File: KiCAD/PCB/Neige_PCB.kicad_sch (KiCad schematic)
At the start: 89 parts, among them J1 TYPE-C 16PIN 2MD(073), SW1 SW_Push, SW10 SW_Push, SW11 SW_Push, SW12 SW_Push, SW13 SW_Push, SW14 SW_Push, SW15 SW_Push, SW16 SW_Push, SW17 SW_Push, SW18 SW_Push, SW19 SW_Push, SW2 SW_Push, SW20 SW_Push, SW21 SW_Push, SW22 SW_Push, SW23 SW_Push, SW24 SW_Push, SW25 SW_Push, SW26 SW_Push, SW27 SW_Push, SW28 SW_Push, SW29 SW_Push, SW3 SW_Push, SW30 SW_Push, SW31 SW_Push, SW32 SW_Push, SW33 SW_Push, SW34 SW_Push, SW35 SW_Push, SW36 SW_Push, SW4 SW_Push, SW5 SW_Push, SW6 SW_Push, SW7 SW_Push, SW8 SW_Push, SW9 SW_Push, U1 USBLC6-2SC6, U2 XC6206P332MR, U3 STM32F072CBU6

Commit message: v1.0
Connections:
- net XIN: no longer names the net of U3.5 (PF0)
- net XOUT: no longer names the net of U3.6 (PF1)
- no-connect marks 20 -> 22
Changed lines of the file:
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@@
+	)
+	(no_connect
+		(at 203.2 161.29)
 	)
 	(no_connect
@@
 	(no_connect
 		(at 203.2 184.15)
+	)
+	(no_connect
+		(at 203.2 158.75)
 	)
 	(no_connect
@@
 		)
 	)
-	(global_label "XOUT"
-		(shape input)
-		(at 203.2 161.29 180)
+	(global_label "COL8"
+		(shape input)
+		(at 203.2 176.53 180)
 		(fields_autoplaced yes)
 		(effects
@@
 		)
 		(property "Intersheetrefs" "${INTERSHEET_REFS}"
-			(at 195.4561 161.29 0)
+			(at 195.3767 176.53 0)
 			(effects
 				(font
@@
 		)
 	)
+	(global_label "COL7"
+		(shape input)
+		(at 191.77 33.02 90)
+		(fields_autoplaced yes)
+		(effects
+			(font
+				(size 1.27 1.27)
+			)
+			(justify left)
+		)
+		(property "Intersheetrefs" "${INTERSHEET_REFS}"
+			(at 191.77 25.1967 90)
+			(effects
+				(font
+					(size 1.27 1.27)
+				)
+				(justify left)
+				(hide yes)
+			)
+		)
+	)
+	(global_label "COL11"
+		(shape input)
+		(at 283.21 33.02 90)
+		(fields_autoplaced yes)
+		(effects
+			(font
+				(size 1.27 1.27)
+			)
+			(justify left)
+		)
+		(property "Intersheetrefs" "${INTERSHEET_REFS}"
+			(at 283.21 23.9872 90)
+			(effects
+				(font
+					(size 1.27 1.27)
+				)
+				(justify left)
+				(hide yes)
+			)
+		)
+	)
 	(global_label "COL8"
 		(shape input)
-		(at 203.2 176.53 180)
+		(at 214.63 33.02 90)
+		(fields_autoplaced yes)
+		(effects
+			(font
+				(size 1.27 1.27)
+			)
+			(justify left)
+		)
+		(property "Intersheetrefs" "${INTERSHEET_REFS}"
+			(at 214.63 25.1967 90)
+			(effects
+				(font
+					(size 1.27 1.27)
+				)
+				(justify left)
+				(hide yes)
+			)
+		)
+	)
+	(global_label "COL2"
+		(shape input)
+		(at 77.47 33.02 90)
+		(fields_autoplaced yes)
+		(effects
+			(font
+				(size 1.27 1.27)
+			)
+			(justify left)
+		)
+		(property "Intersheetrefs" "${INTERSHEET_REFS}"
+			(at 77.3906 25.7688 90)
+			(effects
+				(font
+					(size 1.27 1.27)
+				)
+				(justify left)
+				(hide yes)
+			)
+		)
+	)
+	(global_label "COL5"
+		(shape input)
+		(at 146.05 33.02 90)
+		(fields_autoplaced yes)
+		(effects
+			(font
+				(size 1.27 1.27)
+			)
+			(justify left)
+		)
+		(property "Intersheetrefs" "${INTERSHEET_REFS}"
+			(at 146.05 25.1967 90)
+			(effects
+				(font
+					(size 1.27 1.27)
+				)
+				(justify left)
+				(hide yes)
+			)
+		)
+	)
+	(global_label "ROW0"
+		(shape input)
+		(at 27.94 49.53 180)
 		(fields_autoplaced yes)
 		(effects
@@
 		)
 		(property "Intersheetrefs" "${INTERSHEET_REFS}"
-			(at 195.3767 176.53 0)
+			(at 19.6934 49.53 0)
 			(effects
 				(font
@@
 		)
 	)
-	(global_label "COL7"
-		(shape input)
-		(at 191.77 33.02 90)
+	(global_label "COL1"
+		(shape input)
+		(at 54.61 33.02 90)
 		(fields_autoplaced yes)
 		(effects
@@
 		)
 		(property "Intersheetrefs" "${INTERSHEET_REFS}"
-			(at 191.77 25.1967 90)
+			(at 54.5306 25.7688 90)
 			(effects
 				(font
@@
 		)
 	)
-	(global_label "COL11"
-		(shape input)
-		(at 283.21 33.02 90)
+	(global_label "ROW2"
+		(shape input)
+		(at 27.94 82.55 180)
+		(fields_autoplaced yes)
+		(effects
+			(font
+				(size 1.27 1.27)
+			)
+			(justify right)
+		)
+		(property "Intersheetrefs" "${INTERSHEET_REFS}"
+			(at 19.6934 82.55 0)
+			(effects
+				(font
+					(size 1.27 1.27)
+				)
+				(justify right)
+				(hide yes)
+			)
+		)
+	)
+	(global_label "ROW1"
+		(shape input)
+		(at 203.2 181.61 180)
+		(fields_autoplaced yes)
+		(effects
+			(font
+				(size 1.27 1.27)
+			)
+			(justify right)
+		)
+		(property "Intersheetrefs" "${INTERSHEET_REFS}"
+			(at 194.9534 181.61 0)
+			(effects
+				(font
+					(size 1.27 1.27)
+				)
+				(justify right)
+				(hide yes)
+			)
+		)
+	)
+	(global_label "BOOT"
+		(shape input)
+		(at 127 212.09 0)
 		(fields_autoplaced yes)
 		(effects
@@
 		)
 		(property "Intersheetrefs" "${INTERSHEET_REFS}"
-			(at 283.21 23.9872 90)
+			(at 134.8838 212.09 0)
 			(effects
 				(font
@@
 		)
 	)
-	(global_label "COL8"
-		(shape input)
-		(at 214.63 33.02 90)
+	(global_label "COL0"
+		(shape input)
+		(at 31.75 33.02 90)
 		(fields_autoplaced yes)
 		(effects
@@
 		)
 		(property "Intersheetrefs" "${INTERSHEET_REFS}"
-			(at 214.63 25.1967 90)
+			(at 31.6706 25.7688 90)
 			(effects
 				(font
@@
 		)
 	)
-	(global_label "COL2"
-		(shape input)
-		(at 77.47 33.02 90)
+	(global_label "COL10"
+		(shape input)
+		(at 260.35 33.02 90)
 		(fields_autoplaced yes)
 		(effects
@@
 		)
 		(property "Intersheetrefs" "${INTERSHEET_REFS}"
-			(at 77.3906 25.7688 90)
+			(at 260.35 23.9872 90)
 			(effects
 				(font
@@
 				(hide yes)
 			)
-		)
-	)
-	(global_label "COL5"
-		(shape input)
-		(at 146.05 33.02 90)
-		(fields_autoplaced yes)
-		(effects
-			(font
-				(size 1.27 1.27)
-			)
-			(justify left)
-		)
-		(property "Intersheetrefs" "${INTERSHEET_REFS}"
-			(at 146.05 25.1967 90)
-			(effects
-				(font
-					(size 1.27 1.27)
-				)
-				(justify left)
-				(hide yes)
-			)
-		)
-	)
-	(global_label "ROW0"
-		(shape input)
-		(at 27.94 49.53 180)
-		(fields_autoplaced yes)
-		(effects
-			(font
-				(size 1.27 1.27)
-			)
-			(justify right)
-		)
-		(property "Intersheetrefs" "${INTERSHEET_REFS}"
-			(at 19.6934 49.53 0)
-			(effects
-				(font
-					(size 1.27 1.27)
-				)
-				(justify right)
-				(hide yes)
-			)
-		)
-	)
-	(global_label "COL1"
-		(shape input)
-		(at 54.61 33.02 90)
-		(fields_autoplaced yes)
-		(effects
-			(font
-				(size 1.27 1.27)
-			)
-			(justify left)
-		)
-		(property "Intersheetrefs" "${INTERSHEET_REFS}"
-			(at 54.5306 25.7688 90)
-			(effects
-				(font
-					(size 1.27 1.27)
-				)
-				(justify left)
-				(hide yes)
-			)
-		)
-	)
-	(global_label "ROW2"
-		(shape input)
-		(at 27.94 82.55 180)
-		(fields_autoplaced yes)
-		(effects
-			(font
-				(size 1.27 1.27)
-			)
-			(justify right)
-		)
-		(property "Intersheetrefs" "${INTERSHEET_REFS}"
-			(at 19.6934 82.55 0)
-			(effects
-				(font
-					(size 1.27 1.27)
-				)
-				(justify right)
-				(hide yes)
-			)
-		)
-	)
-	(global_label "ROW1"
-		(shape input)
-		(at 203.2 181.61 180)
-		(fields_autoplaced yes)
-		(effects
-			(font
-				(size 1.27 1.27)
-			)
-			(justify right)
-		)
-		(property "Intersheetrefs" "${INTERSHEET_REFS}"
-			(at 194.9534 181.61 0)
-			(effects
-				(font
-					(size 1.27 1.27)
-				)
-				(justify right)
-				(hide yes)
-			)
-		)
-	)
-	(global_label "BOOT"
-		(shape input)
-		(at 127 212.09 0)
-		(fields_autoplaced yes)
-		(effects
-			(font
-				(size 1.27 1.27)
-			)
-			(justify left)
-		)
-		(property "Intersheetrefs" "${INTERSHEET_REFS}"
-			(at 134.8838 212.09 0)
-			(effects
-				(font
-					(size 1.27 1.27)
-				)
-				(justify left)
-				(hide yes)
-			)
-		)
-	)
-	(global_label "COL0"
-		(shape input)
-		(at 31.75 33.02 90)
-		(fields_autoplaced yes)
-		(effects
-			(font
-				(size 1.27 1.27)
-			)
-			(justify left)
-		)
-		(property "Intersheetrefs" "${INTERSHEET_REFS}"
-			(at 31.6706 25.7688 90)
-			(effects
-				(font
-					(size 1.27 1.27)
-				)
-				(justify left)
-				(hide yes)
-			)
-		)
-	)
-	(global_label "COL10"
-		(shape input)
-		(at 260.35 33.02 90)
-		(fields_autoplaced yes)
-		(effects
-			(font
-				(size 1.27 1.27)
-			)
-			(justify left)
-		)
-		(property "Intersheetrefs" "${INTERSHEET_REFS}"
-			(at 260.35 23.9872 90)
-			(effects
-				(font
-					(size 1.27 1.27)
-				)
-				(justify left)
-				(hide yes)
-			)
-		)
-	)
-	(global_label "XIN"
-		(shape input)
-		(at 203.2 158.75 180)
-		(fields_autoplaced yes)
-		(effects
-			(font
-				(size 1.27 1.27)
-			)
-			(justify right)
-		)
-		(property "Intersheetrefs" "${INTERSHEET_REFS}"
-			(at 197.1494 158.75 0)
-			(effects
-				(font
-					(size 1.27 1.27)
-				)
-				(justify right)
-				(hide yes)
-			)

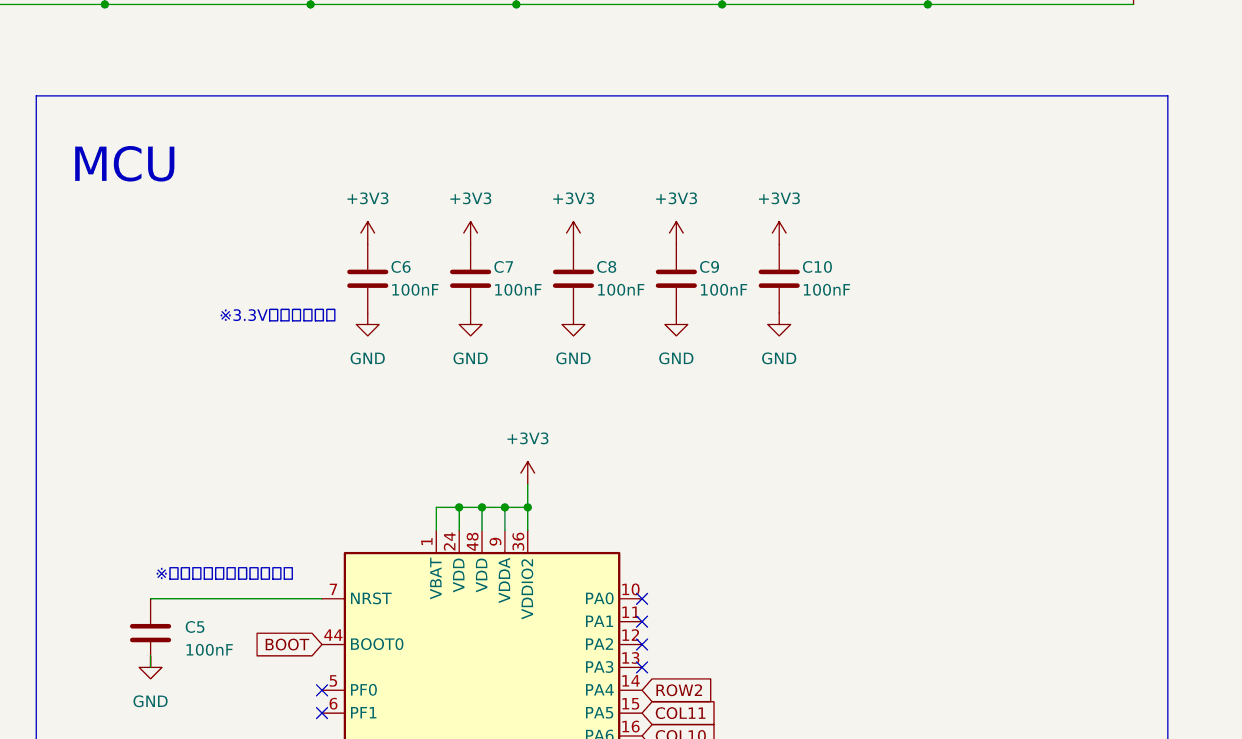
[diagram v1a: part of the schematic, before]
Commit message: パスコン見直し版
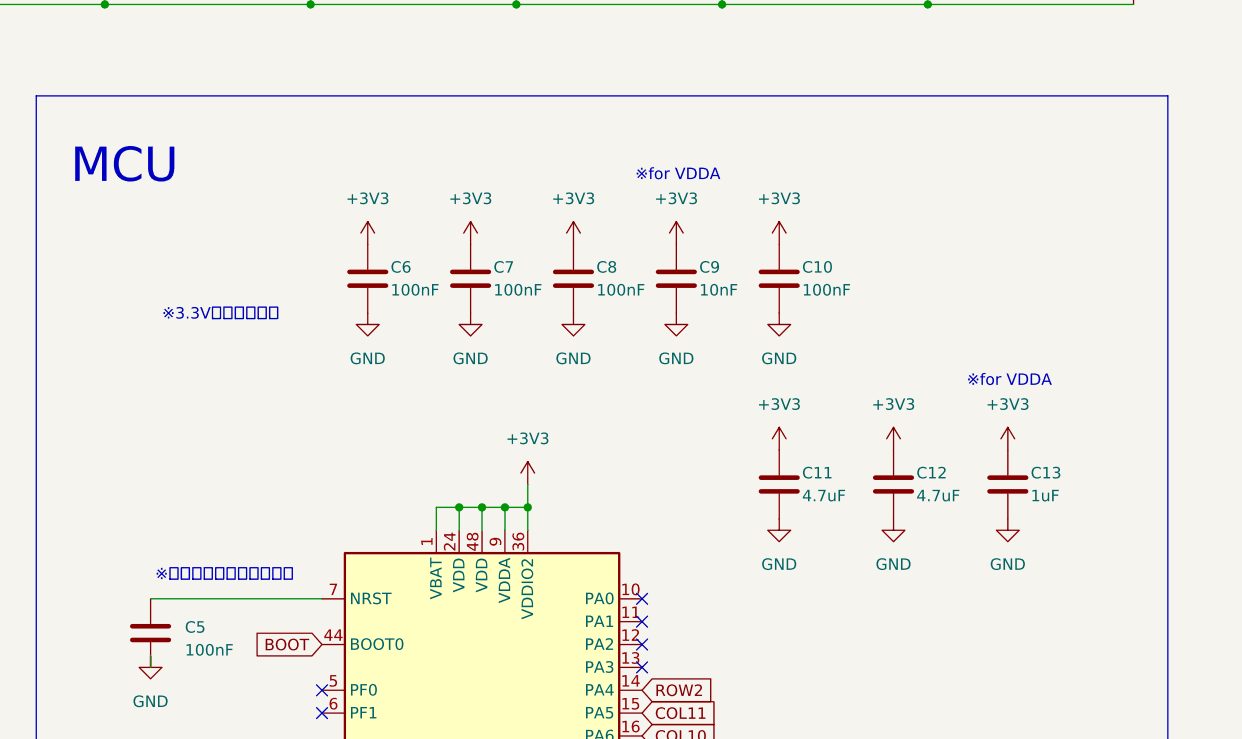
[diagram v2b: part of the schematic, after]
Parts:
- added C11, C12: 4.7uF, Capacitor_SMD:C_0402_1005Metric, symbol Device:C
- added C13: 1uF, Capacitor_SMD:C_0402_1005Metric, symbol Device:C
- C9: value 100nF -> 10nF; JLCPCB Part # C1525 -> C15195
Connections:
- net +3V3: now also C11.1, C12.1, C13.1
- net GND: now also C11.2, C12.2, C13.2
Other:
- note added: "※for VDDA"
- title: Neige PCB -> neige PCB
